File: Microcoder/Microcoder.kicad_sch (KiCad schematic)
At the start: 7 parts, among them IC101 AS5600-ASOT, J101 Conn_01x04

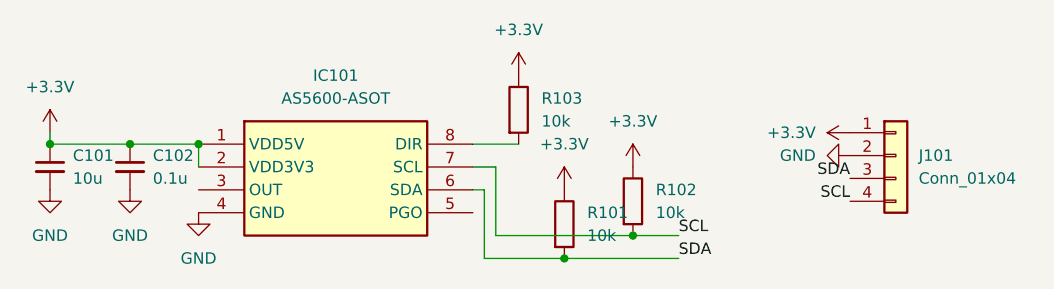
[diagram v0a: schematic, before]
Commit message: Fixed issues preparing for build
Fixed XT30 connectors on Hydra_Driver reversed, fixed I2C connector pin order, refined silkscreens
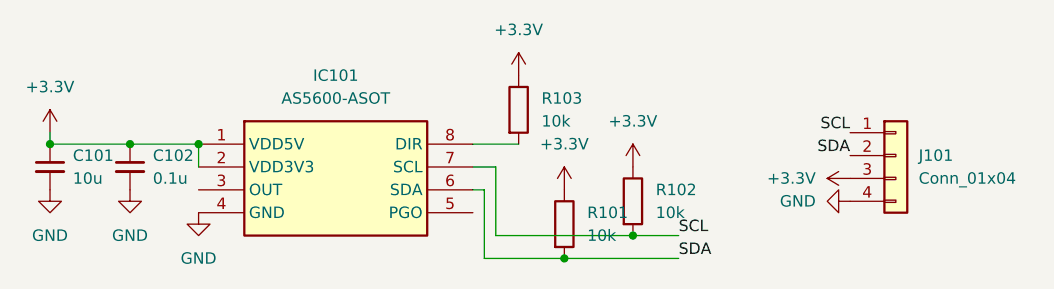
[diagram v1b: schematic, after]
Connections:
- net +3.3V: now also J101.3 (Pin_3); no longer J101.1 (Pin_1)
- net GND: now also J101.4 (Pin_4); no longer J101.2 (Pin_2)
- net SCL: now also J101.1 (Pin_1); no longer J101.4 (Pin_4)
- net SDA: now also J101.2 (Pin_2); no longer J101.3 (Pin_3)
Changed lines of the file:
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@@
 	)
 	(label "SDA"
-		(at 115.57 39.37 180)
+		(at 115.57 36.83 180)
 		(effects
 			(font
@@
 	)
 	(label "SCL"
-		(at 115.57 41.91 180)
+		(at 115.57 34.29 180)
 		(effects
 			(font
@@
 	(symbol
 		(lib_id "power:GND")
-		(at 115.57 36.83 270)
+		(at 115.57 41.91 270)
 		(unit 1)
 		(exclude_from_sim no)
@@
 		(fields_autoplaced yes)
 		(property "Reference" "#PWR0110"
-			(at 109.22 36.83 0)
+			(at 109.22 41.91 0)
 			(effects
 				(font
@@
 		)
 		(property "Value" "GND"
-			(at 111.76 36.8299 90)
+			(at 111.76 41.9099 90)
 			(effects
 				(font
@@
 		)
 		(property "Footprint" ""
-			(at 115.57 36.83 0)
+			(at 115.57 41.91 0)
 			(effects
 				(font
@@
 		)
 		(property "Datasheet" ""
-			(at 115.57 36.83 0)
+			(at 115.57 41.91 0)
 			(effects
 				(font
@@
 		)
 		(property "Description" "Power symbol creates a global label with name \"GND\" , ground"
-			(at 115.57 36.83 0)
+			(at 115.57 41.91 0)
 			(effects
 				(font
@@
 	(symbol
 		(lib_id "power:+3.3V")
-		(at 115.57 34.29 90)
+		(at 115.57 39.37 90)
 		(unit 1)
 		(exclude_from_sim no)
@@
 		(fields_autoplaced yes)
 		(property "Reference" "#PWR0109"
-			(at 119.38 34.29 0)
+			(at 119.38 39.37 0)
 			(effects
 				(font
@@
 		)
 		(property "Value" "+3.3V"
-			(at 111.76 34.2899 90)
+			(at 111.76 39.3699 90)
 			(effects
 				(font
@@
 		)
 		(property "Footprint" ""
-			(at 115.57 34.29 0)
+			(at 115.57 39.37 0)
 			(effects
 				(font
@@
 		)
 		(property "Datasheet" ""
-			(at 115.57 34.29 0)
+			(at 115.57 39.37 0)
 			(effects
 				(font
@@
 		)
 		(property "Description" "Power symbol creates a global label with name \"+3.3V\""
-			(at 115.57 34.29 0)
-			(effects
-				(font
+			(at 115.57 39.37 0)
+			(effects
+				(font

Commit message: More changes to start production
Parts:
- removed R103: 10k, Resistor_SMD:R_0402_1005Metric, symbol Device:R
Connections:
- net GND: now also IC101.8 (DIR)
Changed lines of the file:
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@@
-	(wire
-		(pts
-			(xy 73.66 35.56) (xy 78.74 35.56)
-		)
-		(stroke
-			(width 0)
-			(type default)
-		)
-	)
 	(wire
 		(pts
@@
 	)
 	(symbol
+		(lib_id "power:GND")
+		(at 73.66 35.56 90)
+		(unit 1)
+		(exclude_from_sim no)
+		(in_bom yes)
+		(on_board yes)
+		(dnp no)
+		(fields_autoplaced yes)
+		(property "Reference" "#PWR0103"
+			(at 80.01 35.56 0)
+			(effects
+				(font
+					(size 1.27 1.27)
+				)
+				(hide yes)
+			)
+		)
+		(property "Value" "GND"
+			(at 77.47 35.5599 90)
+			(effects
+				(font
+					(size 1.27 1.27)
+				)
+				(justify right)
+			)
+		)
+		(property "Footprint" ""
+			(at 73.66 35.56 0)
+			(effects
+				(font
+					(size 1.27 1.27)
+				)
+				(hide yes)
+			)
+		)
+		(property "Datasheet" ""
+			(at 73.66 35.56 0)
+			(effects
+				(font
+					(size 1.27 1.27)
+				)
+				(hide yes)
+			)
+		)
+		(property "Description" "Power symbol creates a global label with name \"GND\" , ground"
+			(at 73.66 35.56 0)
+			(effects
+				(font
+					(size 1.27 1.27)
+				)
+				(hide yes)
+			)
+		)
+		(pin "1"
+		)
+		(instances
+			(project ""
+				(path "/e16511bf-512b-475d-aead-9861d1dac631"
+					(reference "#PWR0103")
+					(unit 1)
+				)
+			)
+		)
+	)
+	(symbol
 		(lib_id "Touchstone:AS5600-ASOT")
 		(at 43.18 35.56 0)
@@
 	(symbol
 		(lib_id "power:+3.3V")
-		(at 78.74 27.94 0)
-		(unit 1)
-		(exclude_from_sim no)
-		(in_bom yes)
-		(on_board yes)
-		(dnp no)
-		(fields_autoplaced yes)
-		(property "Reference" "#PWR0103"
-			(at 78.74 31.75 0)
-			(effects
-				(font
-					(size 1.27 1.27)
-				)
-				(hide yes)
-			)
-		)
-		(property "Value" "+3.3V"
-			(at 78.74 22.86 0)
-			(effects
-				(font
-					(size 1.27 1.27)
-				)
-			)
-		)
-		(property "Footprint" ""
-			(at 78.74 27.94 0)
-			(effects
-				(font
-					(size 1.27 1.27)
-				)
-				(hide yes)
-			)
-		)
-		(property "Datasheet" ""
-			(at 78.74 27.94 0)
-			(effects
-				(font
-					(size 1.27 1.27)
-				)
-				(hide yes)
-			)
-		)
-		(property "Description" "Power symbol creates a global label with name \"+3.3V\""
-			(at 78.74 27.94 0)
-			(effects
-				(font
-					(size 1.27 1.27)
-				)
-				(hide yes)
-			)
-		)
-		(pin "1"
-		)
-		(instances
-			(project "Hydra_Encoder"
-				(path "/e16511bf-512b-475d-aead-9861d1dac631"
-					(reference "#PWR0103")
-					(unit 1)
-				)
-			)
-		)
-	)
-	(symbol
-		(lib_id "power:+3.3V")
 		(at 91.44 38.1 0)
 		(unit 1)
@@
 					(unit 1)
 				)
-			)
-		)
-	)
-	(symbol
-		(lib_id "Device:R")
-		(at 78.74 31.75 0)
-		(unit 1)
-		(exclude_from_sim no)
-		(in_bom yes)
-		(on_board yes)
-		(dnp no)
-		(fields_autoplaced yes)
-		(property "Reference" "R103"
-			(at 81.28 30.4799 0)
-			(effects
-				(font
-					(size 1.27 1.27)
-				)
-				(justify left)
-			)
-		)
-		(property "Value" "10k"
-			(at 81.28 33.0199 0)
-			(effects
-				(font
-					(size 1.27 1.27)
-				)
-				(justify left)
-			)
-		)
-		(property "Footprint" "Resistor_SMD:R_0402_1005Metric"
-			(at 76.962 31.75 90)
-			(effects
-				(font
-					(size 1.27 1.27)
-				)
-				(hide yes)
-			)
-		)
-		(property "Datasheet" "~"
-			(at 78.74 31.75 0)
-			(effects
-				(font
-					(size 1.27 1.27)
-				)
-				(hide yes)
-			)
-		)
-		(property "Description" "Resistor"
-			(at 78.74 31.75 0)
-			(effects
-				(font
-					(size 1.27 1.27)
-				)
-				(hide yes)
-			)
-		)
-		(pin "1"
-		)
-		(pin "2"
-		)
-		(instances
-			(project "Hydra_Encoder"
-				(path "/e16511bf-512b-475d-aead-9861d1dac631"
-					(reference "R103")
-					(unit 1)
-				)
